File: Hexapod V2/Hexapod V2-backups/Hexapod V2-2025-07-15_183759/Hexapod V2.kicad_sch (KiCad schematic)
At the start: 38 parts, among them J1 Battery, J2 Switch, U1 MPU6050, U2 NRF24L01_Breakout, U3 ACS712xLCTR-05B, U4 Teensy 4.1

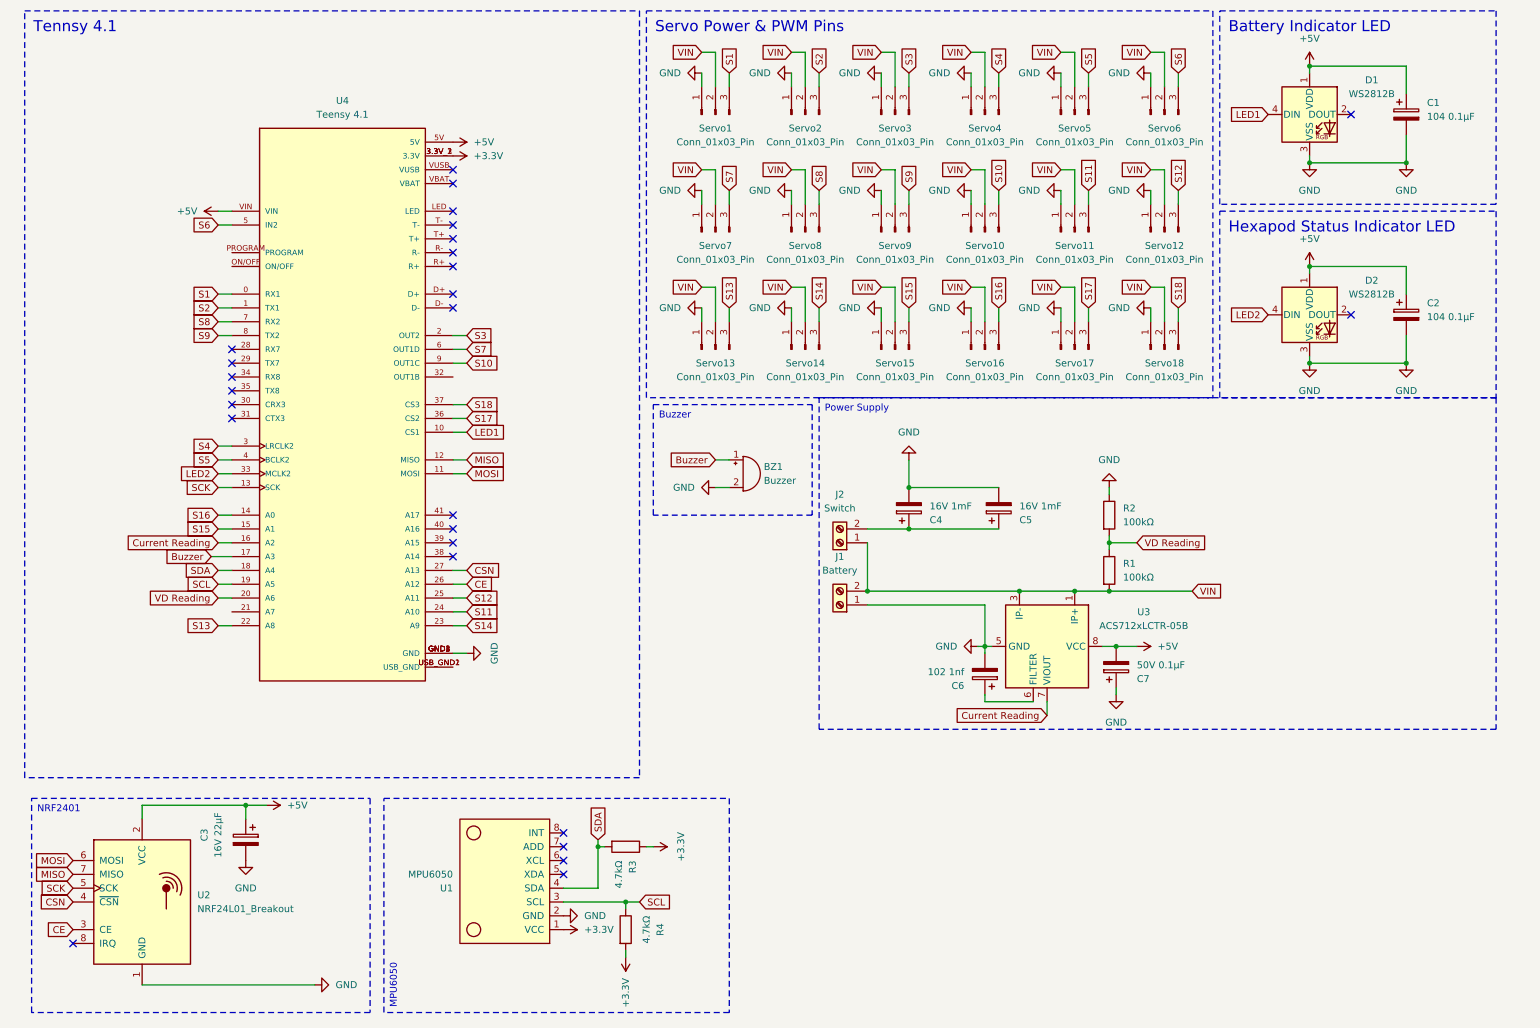
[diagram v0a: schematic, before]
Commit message: Added Teensy
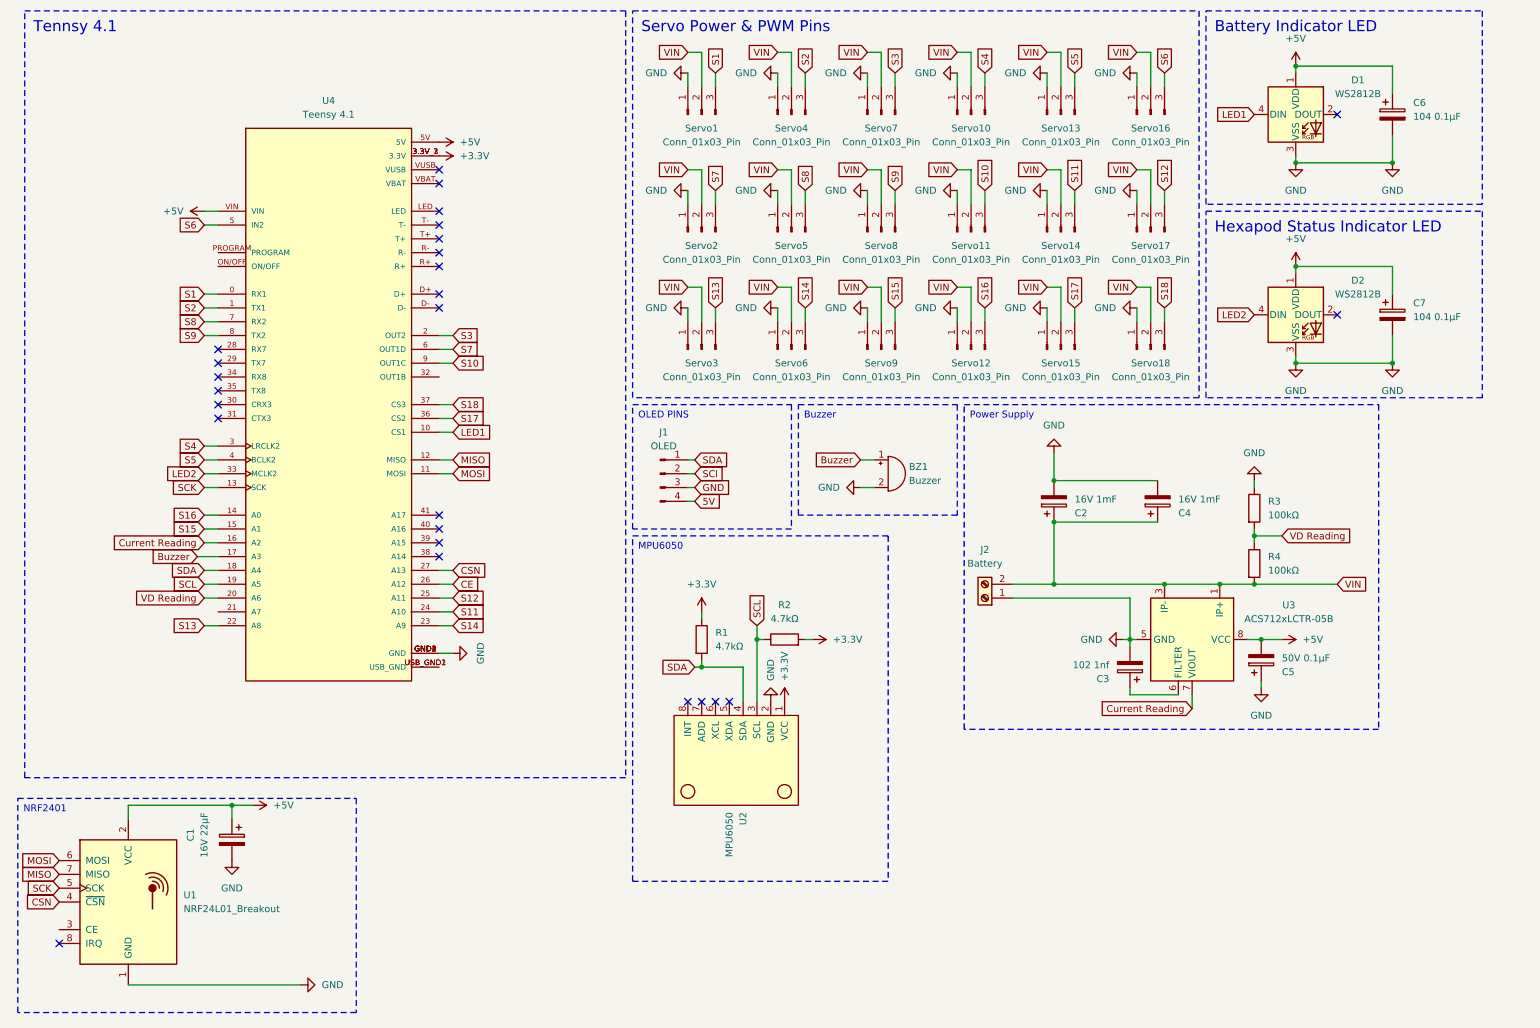
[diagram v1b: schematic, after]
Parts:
- removed J1: Battery, TerminalBlock_Phoenix:TerminalBlock_Phoenix_MKDS-1,5-2-5.08_1x02_P5.08mm_Horizontal, symbol Connector:Screw_Terminal_01x02
- removed U1: MPU6050, usini_sensors:module_mpu6050, symbol Breakout Sensors:module_mpu6050
- removed U2: NRF24L01_Breakout, RF_Module:nRF24L01_Breakout, symbol RF:NRF24L01_Breakout
- added J1: OLED, symbol Connector:Conn_01x04_Pin
- added U1: NRF24L01_Breakout, RF_Module:nRF24L01_Breakout, symbol RF:NRF24L01_Breakout
- added U2: MPU6050, usini_sensors:module_mpu6050, symbol Breakout Sensors:module_mpu6050
- C1: value 104 0.1μF -> 16V 22μF; footprint Capacitor_SMD:C_1206_3216Metric -> Capacitor_THT:CP_Radial_D4.0mm_P2.00mm
- C2: value 104 0.1μF -> 16V 1mF; footprint Capacitor_SMD:C_1206_3216Metric -> Capacitor_THT:CP_Radial_D10.0mm_P7.50mm
- C3: value 16V 22μF -> 102 1nf; footprint Capacitor_THT:CP_Radial_D4.0mm_P2.00mm -> Capacitor_SMD:C_0805_2012Metric
- C5: value 16V 1mF -> 50V 0.1μF; footprint Capacitor_THT:CP_Radial_D10.0mm_P7.50mm -> Capacitor_THT:CP_Radial_D5.0mm_P2.00mm
- C6: value 102 1nf -> 104 0.1μF; footprint Capacitor_SMD:C_0805_2012Metric -> Capacitor_SMD:C_1206_3216Metric
- C7: value 50V 0.1μF -> 104 0.1μF; footprint Capacitor_THT:CP_Radial_D5.0mm_P2.00mm -> Capacitor_SMD:C_1206_3216Metric
- J2: value Switch -> Battery
- R1, R2: value 100kΩ -> 4.7kΩ; footprint Resistor_THT:R_Axial_DIN0207_L6.3mm_D2.5mm_P7.62mm_Horizontal -> Resistor_SMD:R_1206_3216Metric
- R3, R4: value 4.7kΩ -> 100kΩ; footprint Resistor_SMD:R_1206_3216Metric -> Resistor_THT:R_Axial_DIN0207_L6.3mm_D2.5mm_P7.62mm_Horizontal
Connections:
- net +3.3V: now also R1.1, R2.2, U2.1 (VCC); no longer R3.1, R4.2
- net +5V: now also C5.2, C6.1, C7.1, U1.2 (VCC); no longer C2.1, C3.1, C7.2
- net CSN: now also U1.4 (~{CSN})
- net GND: now also C5.1, C7.2, J2.1 (Pin_1), R3.1, J1.3 (Pin_3), U1.1 (GND), U2.2 (GND); no longer C5.2, C7.1, R2.1
- net MISO: now also U1.7 (MISO)
- net MOSI: now also U1.6 (MOSI)
- net S10: now also Servo11.3 (Pin_3); no longer Servo10.3 (Pin_3)
- net S11: now also Servo14.3 (Pin_3); no longer Servo11.3 (Pin_3)
- net S12: now also Servo17.3 (Pin_3); no longer Servo12.3 (Pin_3)
- net S13: now also Servo3.3 (Pin_3); no longer Servo13.3 (Pin_3)
- net S14: now also Servo6.3 (Pin_3); no longer Servo14.3 (Pin_3)
- net S15: now also Servo9.3 (Pin_3); no longer Servo15.3 (Pin_3)
- net S16: now also Servo12.3 (Pin_3); no longer Servo16.3 (Pin_3)
- net S17: now also Servo15.3 (Pin_3); no longer Servo17.3 (Pin_3)
- net S2: now also Servo4.3 (Pin_3); no longer Servo2.3 (Pin_3)
- net S3: now also Servo7.3 (Pin_3); no longer Servo3.3 (Pin_3)
- net S4: now also Servo10.3 (Pin_3); no longer Servo4.3 (Pin_3)
- net S5: now also Servo13.3 (Pin_3); no longer Servo5.3 (Pin_3)
- net S6: now also Servo16.3 (Pin_3); no longer Servo6.3 (Pin_3)
- net S7: now also Servo2.3 (Pin_3); no longer Servo7.3 (Pin_3)
- net S8: now also Servo5.3 (Pin_3); no longer Servo8.3 (Pin_3)
- net S9: now also Servo8.3 (Pin_3); no longer Servo9.3 (Pin_3)
- net SCK: now also U1.5 (SCK)
- net SCL: now also R2.1, U2.3 (SCL); no longer R4.1
- net SDA: now also R1.2, J1.1 (Pin_1), U2.4 (SDA); no longer R3.2
- net VD Reading: now also R3.2, R4.1; no longer R1.1, R2.2
- net VIN: now also C2.1, C4.1, J2.2 (Pin_2), R4.2; no longer J2.1 (Pin_1), R1.2
- net at U3.6 (FILTER): now also C3.1; no longer C6.1
- new net 5V: J1.4 (Pin_4)
- new net SCl: J1.2 (Pin_2)
